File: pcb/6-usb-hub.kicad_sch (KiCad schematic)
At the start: 0 parts

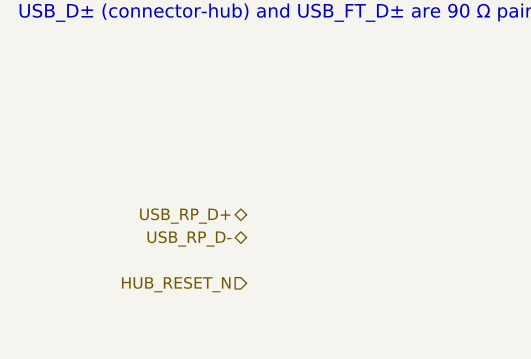
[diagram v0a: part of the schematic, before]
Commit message: Phase 3: populate power sheet; descriptive net names
Power sheet: bench eFuse (TPS259470A) with UVLO/OVLO string and EN
clamp, TPS2116 bench-priority mux with VBUS snubber, 3.3 V and 2.83 V
TPS73701 LDOs. Notes on the string's tap voltages, eFuse setting pins
and every DNP part. Project symbol library with the TPS259470A and
TPS73701DCQ drawn from the datasheet pin tables.

Nets renamed to spelled-out names (IS_BENCH_POWERED, *_INVERTED for
active-low, FEEDBACK, VTERMINATOR, TERMINATOR_EN) across the schematic,
pinout page, parts list and power block page.

Co-Authored-By: Claude Opus 5.5 <noreply@anthropic.com>
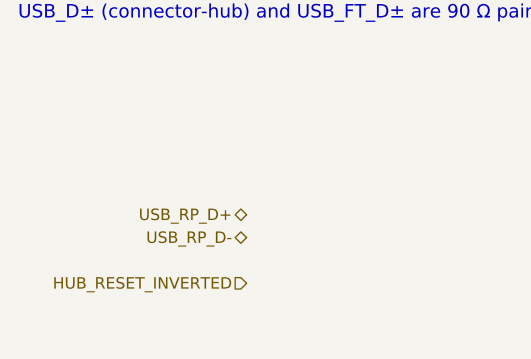
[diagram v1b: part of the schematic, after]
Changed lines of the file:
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@@
 	(hierarchical_label "USB_RP_D+" (shape bidirectional) (at 50.8 50.8 180) (effects (font (size 1.27 1.27)) (justify right)))
 	(hierarchical_label "USB_RP_D-" (shape bidirectional) (at 50.8 53.34 180) (effects (font (size 1.27 1.27)) (justify right)))
-	(hierarchical_label "HUB_RESET_N" (shape input) (at 50.8 58.42 180) (effects (font (size 1.27 1.27)) (justify right)))
+	(hierarchical_label "HUB_RESET_INVERTED" (shape input) (at 50.8 58.42 180) (effects (font (size 1.27 1.27)) (justify right)))
 	(hierarchical_label "USB_FT_D+" (shape bidirectional) (at 343.8 50.8 0) (effects (font (size 1.27 1.27)) (justify left)))
 	(hierarchical_label "USB_FT_D-" (shape bidirectional) (at 343.8 53.34 0) (effects (font (size 1.27 1.27)) (justify left)))
